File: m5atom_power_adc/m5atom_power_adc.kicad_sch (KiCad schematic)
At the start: 101 parts, among them J1 USB_C_Receptacle_USB2.0_14P, J10 Conn_01x02, J2 GROVE-CONNECTOR, J3 Conn_01x04_Pin, J4 Conn_01x02, J5 Conn_01x02, J6 Conn_01x02, J7 Conn_01x02, J8 Conn_01x02, J9 GROVE-CONNECTOR, Q1 AO3401A, Q2 MMBT2222A, Q3 MMBT2222A, Q4 MMBT2222A, Q5 AO3401A, Q6 MMBT2222A, Q7 MMBT2222A, SW1 Boot, SW2 Reset, U1 LM2596S-5, U2 ESP32-S3-MINI-1, U3 AMS1117-3.3, U4 ADS1115IDGS, U5 AMS1117-3.3

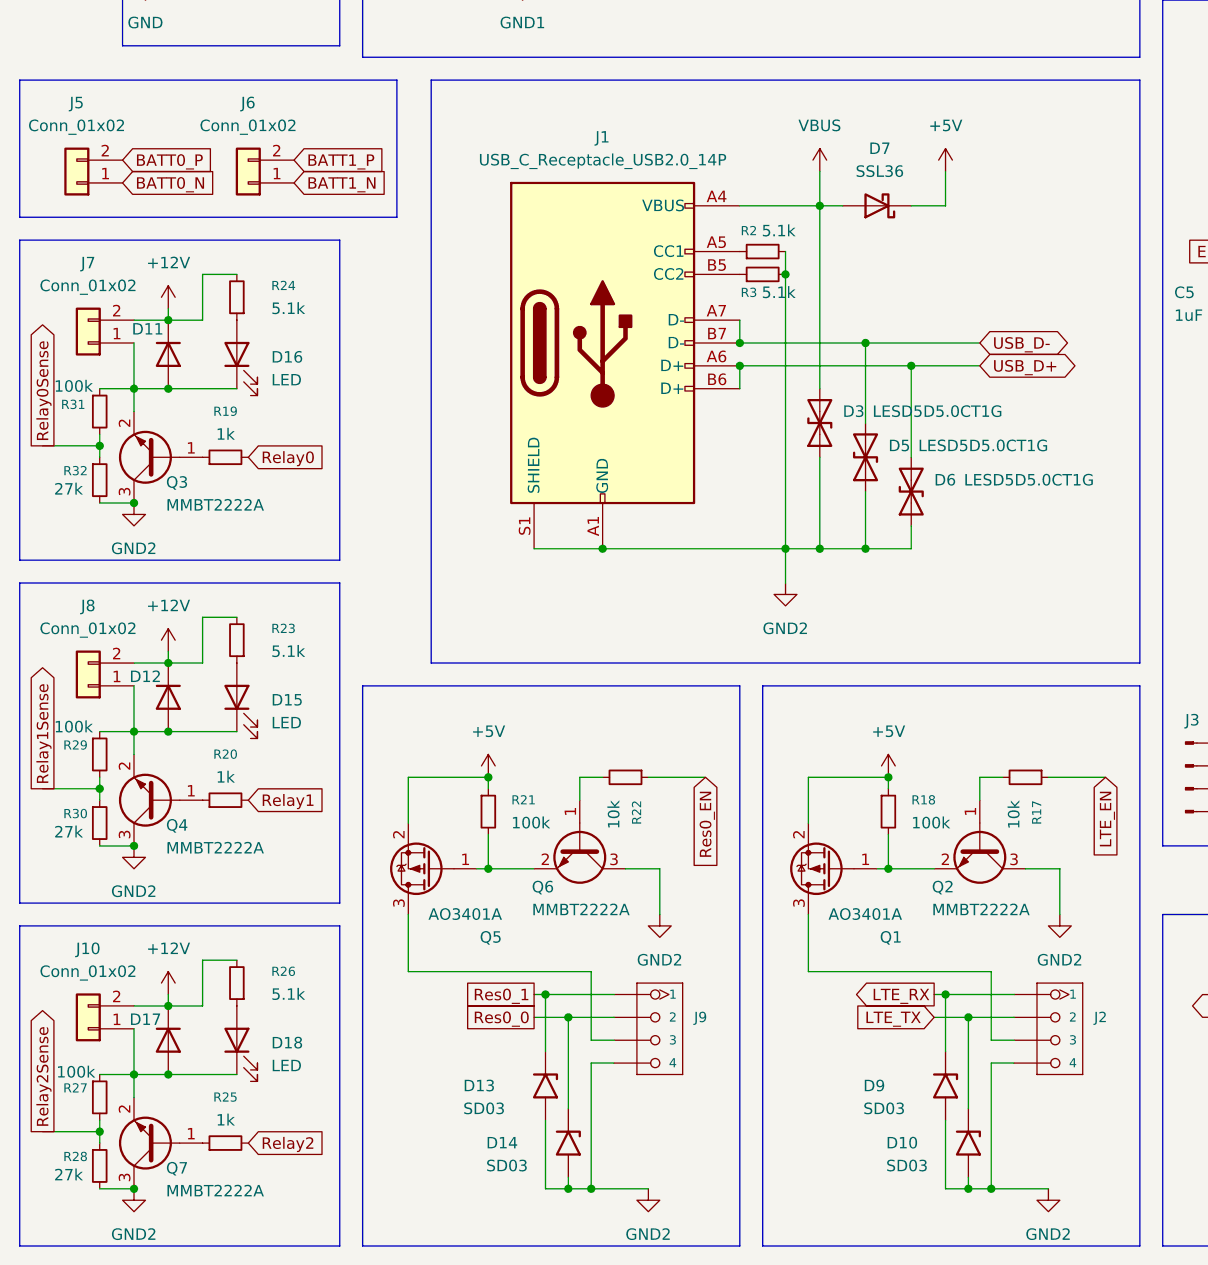
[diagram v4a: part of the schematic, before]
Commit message: fix: トランジスタの向きを修正、外部スイッチ用コネクタ追加
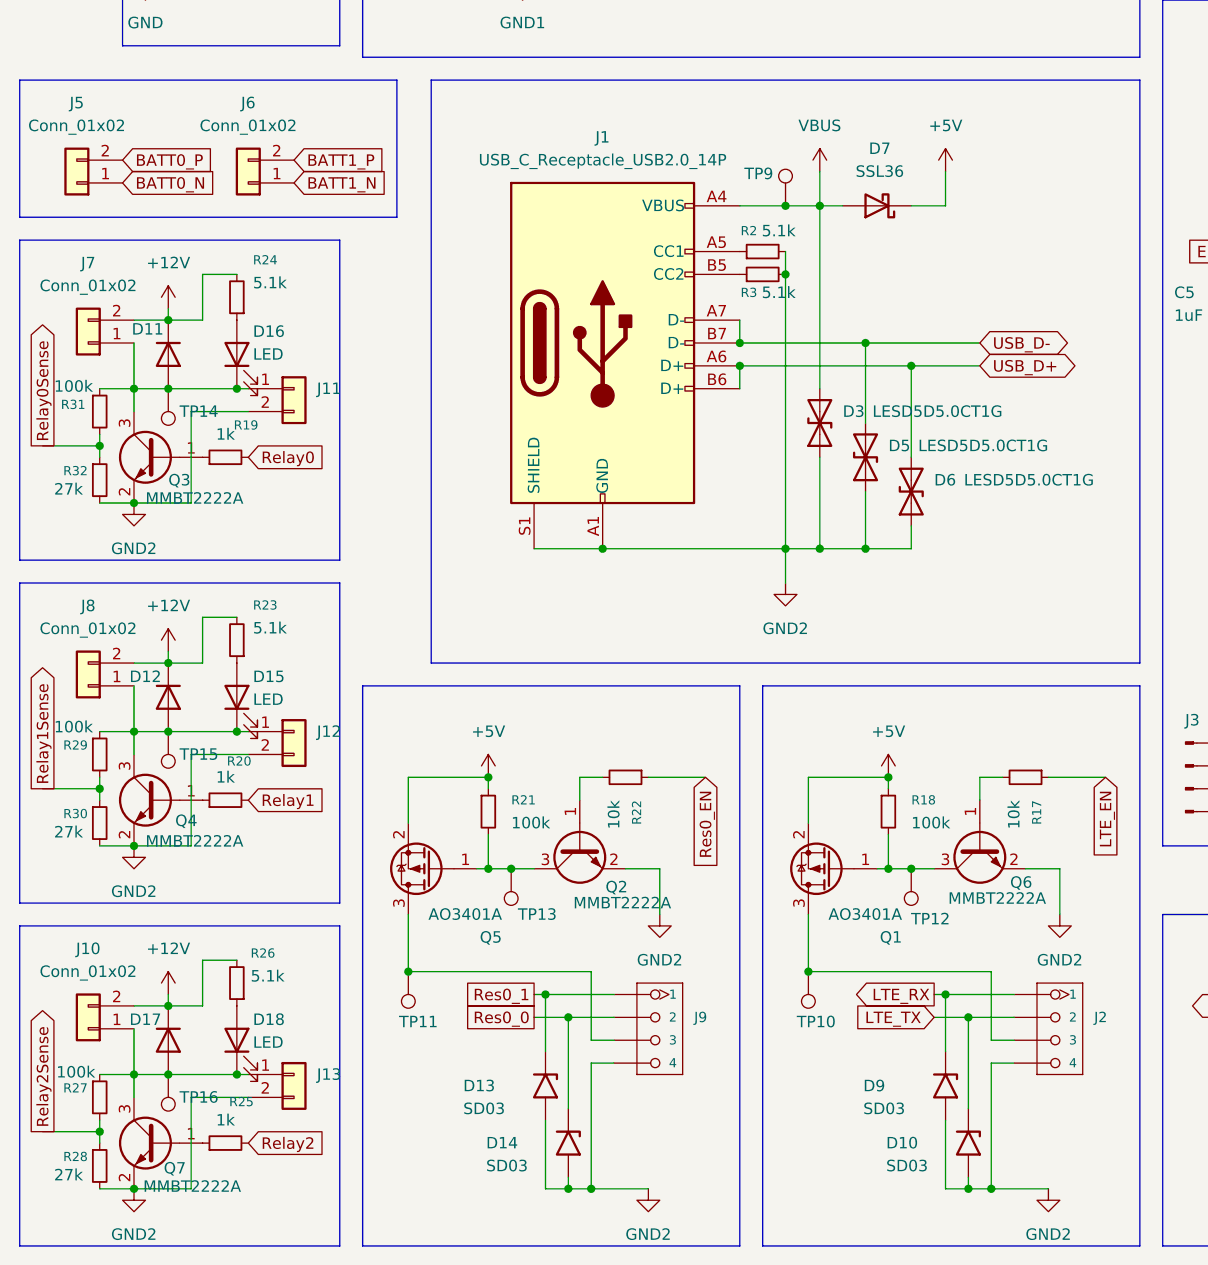
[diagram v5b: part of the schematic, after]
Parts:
- added J11, J12, J13: Conn_01x02, symbol Connector_Generic:Conn_01x02
- added TP10, TP11, TP12, TP13, TP14, TP15, TP16, TP9: TestPoint, TestPoint:TestPoint_Pad_D1.5mm, symbol Connector:TestPoint
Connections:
- net GND: now also Q2.2 (E), Q3.2 (E), Q4.2 (E), Q6.2 (E), Q7.2 (E), J11.2 (Pin_2), J12.2 (Pin_2), J13.2 (Pin_2); no longer Q2.3 (C), Q3.3 (C), Q4.3 (C), Q6.3 (C), Q7.3 (C)
- net VBUS: now also TP9.1
- net at D11.2 (A), D16.1 (K), J7.1 (Pin_1)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: now also Q3.3 (C), J11.1 (Pin_1), TP14.1; no longer Q3.2 (E)
- net at D17.2 (A), D18.1 (K), J10.1 (Pin_1)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: now also Q7.3 (C), J13.1 (Pin_1), TP16.1; no longer Q7.2 (E)
- net at Q6.1 (B): now also R17.2; no longer R22.2
- net at Q5.1 (G), R21.2: now also Q2.3 (C), TP13.1; no longer Q6.2 (E)
- net at J9.3, Q5.3 (D): now also TP11.1
- net at D12.2 (A), D15.1 (K), J8.1 (Pin_1)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: now also Q4.3 (C), J12.1 (Pin_1), TP15.1; no longer Q4.2 (E)
- net at Q1.1 (G), R18.2: now also Q6.3 (C), TP12.1; no longer Q2.2 (E)
- net at J2.3, Q1.3 (D): now also TP10.1
- net at Q2.1 (B): now also R22.2; no longer R17.2
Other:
- moved on the sheet: Q2, Q3, Q4, Q6, Q7
